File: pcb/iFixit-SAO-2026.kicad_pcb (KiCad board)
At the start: 2 copper layers, 82.6 x 83.8 mm, 11 parts

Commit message: Update from our April 29th meeting.
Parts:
- added R1: 65R, Resistor_SMD:R_1206_3216Metric_Pad1.30x1.75mm_HandSolder, B.Cu at (108.6, 172.3)
- added R2: 65Ω, Resistor_SMD:R_1206_3216Metric_Pad1.30x1.75mm_HandSolder, B.Cu at (108.6, 168.3)
- added TP1: SAO Tether, TestPoint:TestPoint_Keystone_5019_Miniature, B.Cu at (86.7, 158.4)
- added U1: ATtiny1604-SS, Package_SO:SOIC-14_3.9x8.7mm_P1.27mm, B.Cu at (111.4, 147.7)
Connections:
- D1 pad 1: unconnected-(D1-K-Pad1) -> Net-(D1-K)
- D1 pad 2: unconnected-(D1-A-Pad2) -> Net-(D1-A)
- D2 pad 1: unconnected-(D2-K-Pad1) -> Net-(D2-K)
- D2 pad 2: unconnected-(D2-A-Pad2) -> Net-(D2-A)
- LED1 pad 2: unconnected-(LED1-VDD-Pad2) -> Net-(LED1-VDD)
- LED1 pad 4: unconnected-(LED1-GND-Pad4) -> GND
- LED2 pad 2: unconnected-(LED2-VDD-Pad2) -> Net-(LED1-VDD)
- LED2 pad 4: unconnected-(LED2-GND-Pad4) -> GND
- LED3 pad 2: unconnected-(LED3-VDD-Pad2) -> Net-(LED1-VDD)
- LED3 pad 4: unconnected-(LED3-GND-Pad4) -> GND
- LED4 pad 2: unconnected-(LED4-VDD-Pad2) -> Net-(LED1-VDD)
- LED4 pad 4: unconnected-(LED4-GND-Pad4) -> GND
- LED5 pad 2: unconnected-(LED5-VDD-Pad2) -> Net-(LED1-VDD)
- LED5 pad 4: unconnected-(LED5-GND-Pad4) -> GND
- LED6 pad 2: unconnected-(LED6-VDD-Pad2) -> Net-(LED1-VDD)
- LED6 pad 4: unconnected-(LED6-GND-Pad4) -> GND
- LED7 pad 2: unconnected-(LED7-VDD-Pad2) -> Net-(LED1-VDD)
- LED7 pad 4: unconnected-(LED7-GND-Pad4) -> GND
- SAO1 pad 1: unconnected-(SAO1-3.3V-Pad1) -> Net-(LED1-VDD)
- SAO1 pad 2: unconnected-(SAO1-GND-Pad2) -> GND
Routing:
- net Net-(LED1-VDD): track 0.00 -> 69.8 mm, vias 0 -> 3
- net Net-(D2-A): track 0.00 -> 24.4 mm
- net Net-(D1-A): track 0.00 -> 20.3 mm
- net Net-(D2-K): track 0.00 -> 3.95 mm
- net Net-(D1-K): track 0.00 -> 3.59 mm
- added copper zone on B.Cu, net GND
- added copper zone on F.Cu, net GND

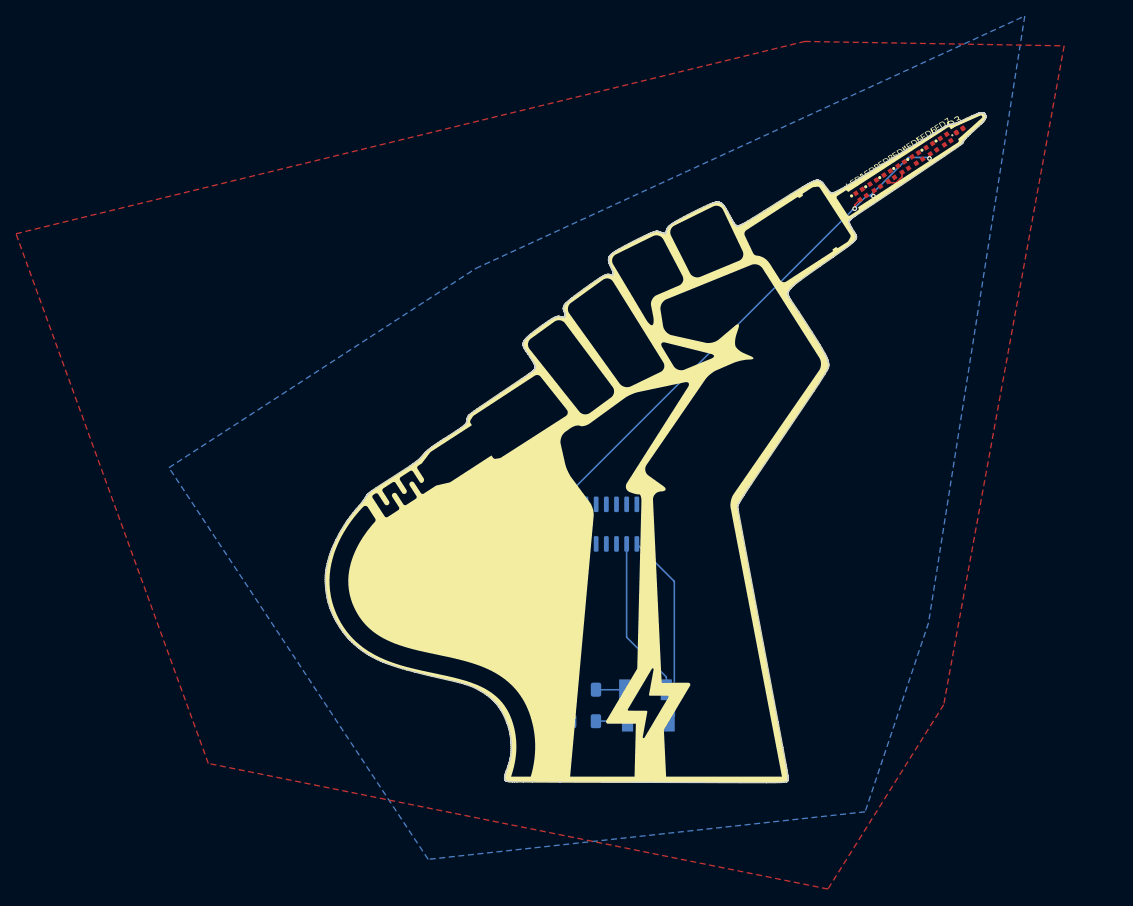
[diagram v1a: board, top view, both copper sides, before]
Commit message: A complete prototype of v0 of the badge, ready for production and assembly. Cleaned up the schematic quite a bit, added teh UDPI programming pads, and updated the SK6508 footprint silkscreen.
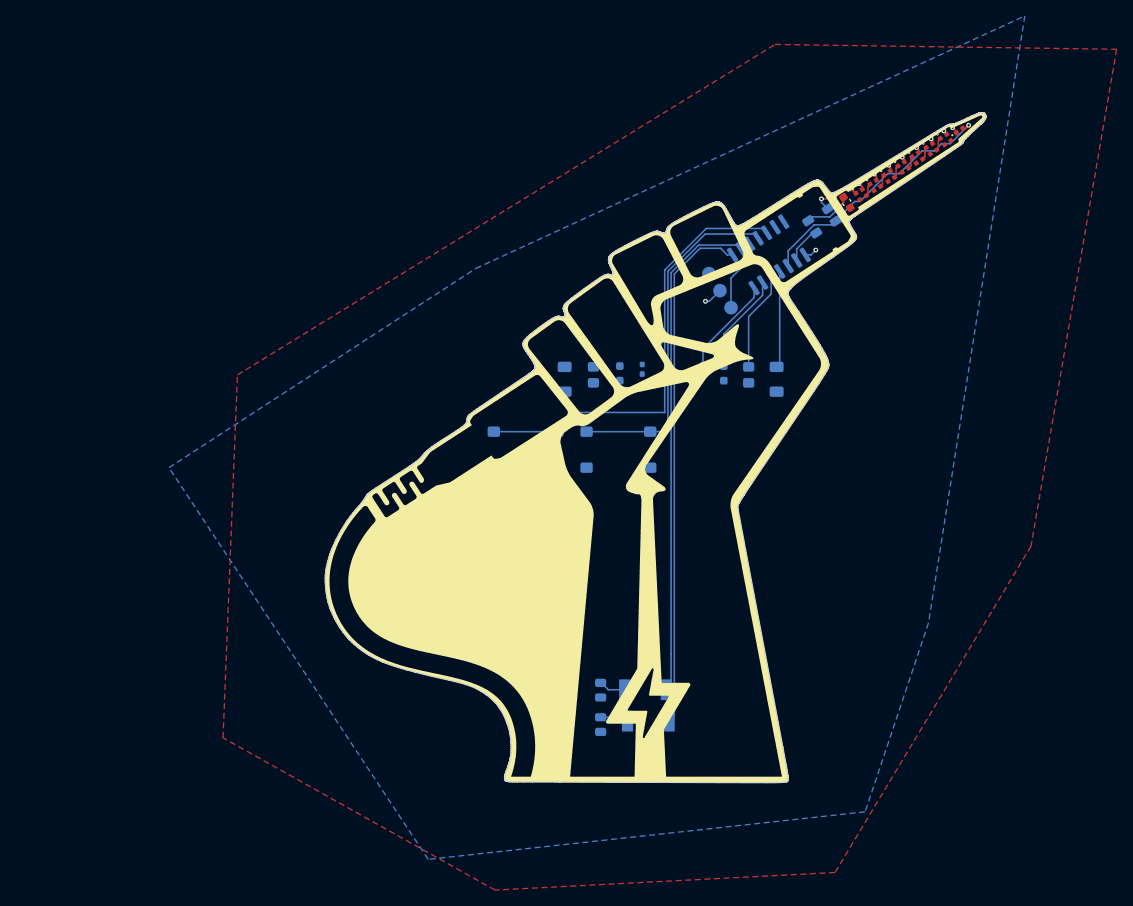
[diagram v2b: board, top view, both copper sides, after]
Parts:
- added C1: 0.1uF, Capacitor_SMD:C_0603_1608Metric, F.Cu at (141.5, 107.5)
- added C2: 0.1uF, Capacitor_SMD:C_0603_1608Metric, B.Cu at (86.7, 158.5)
- added J1: Conn_01x03_Pin, iFixit-SAO-2026:UDPI_1x03_P2.54mm_SMT, B.Cu at (127.0, 120.6)
- added R10: 0R, Resistor_SMD:R_0603_1608Metric_Pad0.98x0.95mm_HandSolder, B.Cu at (113.1, 128.8)
- added R11: R, Resistor_SMD:R_0402_1005Metric_Pad0.72x0.64mm_HandSolder, B.Cu at (123.5, 128.3)
- added R12: 0R, Resistor_SMD:R_0402_1005Metric_Pad0.72x0.64mm_HandSolder, B.Cu at (115.9, 128.3)
- added R3: 500R, Resistor_SMD:R_0805_2012Metric, B.Cu at (139.6, 109.0)
- added R4: 65R, Resistor_SMD:R_0805_2012Metric, B.Cu at (137.1, 110.5)
- added R5: R, Resistor_SMD:R_1206_3216Metric_Pad1.30x1.75mm_HandSolder, B.Cu at (132.7, 129.6)
- added R6: 0R, Resistor_SMD:R_1206_3216Metric_Pad1.30x1.75mm_HandSolder, B.Cu at (106.2, 129.6)
- added R7: R, Resistor_SMD:R_0805_2012Metric_Pad1.20x1.40mm_HandSolder, B.Cu at (129.2, 129.0)
- added R8: 0R, Resistor_SMD:R_0805_2012Metric_Pad1.20x1.40mm_HandSolder, B.Cu at (109.8, 129.0)
- added R9: R, Resistor_SMD:R_0603_1608Metric_Pad0.98x0.95mm_HandSolder, B.Cu at (126.1, 128.8)
- added SW1: SW_Push, Button_Switch_SMD:SW_SPST_PTS645Sx43SMTR92, B.Cu at (112.9, 138.3)
- added SW2: SW_Push, Button_Switch_SMD:SW_SPST_PTS645Sx43SMTR92, B.Cu at (101.3, 138.3)
- R1: renamed from R2; footprint Resistor_SMD:R_1206_3216Metric_Pad1.30x1.75mm_HandSolder -> Resistor_SMD:R_0805_2012Metric
- R2: renamed from R1; footprint Resistor_SMD:R_1206_3216Metric_Pad1.30x1.75mm_HandSolder -> Resistor_SMD:R_0805_2012Metric
- moved U1 39.3 mm to (131.7, 114.0), turned to 123 degrees
- moved TP1 20.1 mm to (106.8, 158.5)
- moved R2 2.18 mm to (110.7, 172.7), turned to -90 degrees
- moved R1 2.13 mm to (110.7, 168.4), turned to -90 degrees
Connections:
- net Net-(LED1-VDD) renamed /3V3
- D3 pad 1: unconnected-(D3-K-Pad1) -> GND
- D3 pad 2: unconnected-(D3-A-Pad2) -> Net-(D3-A)
- LED1 pad 1: unconnected-(LED1-DIN-Pad1) -> /Neopixels
- LED1 pad 3: unconnected-(LED1-DOUT-Pad3) -> Net-(LED1-DOUT)
- LED2 pad 1: unconnected-(LED2-DIN-Pad1) -> Net-(LED1-DOUT)
- LED2 pad 3: unconnected-(LED2-DOUT-Pad3) -> Net-(LED2-DOUT)
- LED3 pad 1: unconnected-(LED3-DIN-Pad1) -> Net-(LED2-DOUT)
- LED3 pad 3: unconnected-(LED3-DOUT-Pad3) -> Net-(LED3-DOUT)
- LED4 pad 1: unconnected-(LED4-DIN-Pad1) -> Net-(LED3-DOUT)
- LED4 pad 3: unconnected-(LED4-DOUT-Pad3) -> Net-(LED4-DOUT)
- LED5 pad 1: unconnected-(LED5-DIN-Pad1) -> Net-(LED4-DOUT)
- LED5 pad 3: unconnected-(LED5-DOUT-Pad3) -> Net-(LED5-DOUT)
- LED6 pad 1: unconnected-(LED6-DIN-Pad1) -> Net-(LED5-DOUT)
- LED6 pad 3: unconnected-(LED6-DOUT-Pad3) -> Net-(LED6-DOUT)
- LED7 pad 1: unconnected-(LED7-DIN-Pad1) -> Net-(LED6-DOUT)
- U1 pad 10: unconnected-(U1-~{RESET}/PA0-Pad10) -> Net-(J1-Pin_1)
- U1 pad 11: unconnected-(U1-PA1-Pad11) -> /BTN1
- U1 pad 12: unconnected-(U1-PA2-Pad12) -> /BTN2
- U1 pad 2: unconnected-(U1-PA4-Pad2) -> Net-(U1-PA4)
- U1 pad 3: unconnected-(U1-PA5-Pad3) -> Net-(U1-PA5)
- U1 pad 4: unconnected-(U1-PA6-Pad4) -> /1206
- U1 pad 5: unconnected-(U1-PA7-Pad5) -> /0805
- U1 pad 6: unconnected-(U1-PB3-Pad6) -> /0603
- U1 pad 7: unconnected-(U1-PB2-Pad7) -> /0402
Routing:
- net /3V3: track 69.8 -> 11.2 mm, vias 3 -> 2
- net /BTN2: track 0.00 -> 55.3 mm
- net /BTN1: track 0.00 -> 43.6 mm
- net Net-(D1-A): track 20.3 -> 63.1 mm
- net Net-(D2-A): track 24.4 -> 65.1 mm
- net Net-(D3-A): track 0.00 -> 25.9 mm, vias 0 -> 1
- net /0603: track 0.00 -> 12.4 mm
- net /0805: track 0.00 -> 12.4 mm
- net /0402: track 0.00 -> 12.2 mm
- net /1206: track 0.00 -> 12.1 mm
- net Net-(U1-PA5): track 0.00 -> 9.39 mm
- net Net-(J1-Pin_1): track 0.00 -> 8.94 mm
- net GND: track 0.00 -> 7.44 mm, vias 0 -> 9
- net /Neopixels: track 0.00 -> 6.46 mm, vias 0 -> 1
- net Net-(U1-PA4): track 0.00 -> 4.70 mm
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- added copper zone on F.Cu, net /3V3
- removed copper zone on F.Cu, net GND
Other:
- board text added: "iFixit SAO 2026 v0"

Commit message: Version v0 sent for PCBA prototype.
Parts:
- R1: value 65Ω -> 65R
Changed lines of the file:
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@@
 			(net "unconnected-(U1-PA3-Pad13)")
 			(pinfunction "PA3_13")
-			(pintype "bidirectional")
+			(pintype "bidirectional+no_connect")
 		)
 		(pad "14" smd roundrect
@@
 			)
 		)
-		(property "Value" "65Ω"
+		(property "Value" "65R"
 			(at 0 -1.65 90)
 			(layer "B.Fab")

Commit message: Version 0.1 (fixed split ground planes, removed button, added new graphics); initial commit of firmware; adding individual pcb layer svgs
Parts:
- removed SW2: SW_Push, Button_Switch_SMD:SW_SPST_PTS645Sx43SMTR92
- moved SW1 11.6 mm to (101.3, 138.3)
- renumbered J1 to UPDI
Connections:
- U1 pad 12: /BTN2 -> unconnected-(U1-PA2-Pad12)
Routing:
- net /BTN2: track 55.3 -> 0.00 mm
- net /BTN1: track 43.6 -> 55.5 mm
- net /0402: track 12.2 -> 17.4 mm
- net /0603: track 12.4 -> 15.3 mm
- net /0805: track 12.4 -> 12.9 mm
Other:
- board text added: "Move these..."
- board text added: "Powering Your Right To Repair"
- board text added: "for a treat."
- board text added: "github.com/NerdFlare/iFixit-SAO-2026"
- board text added: "ifixit.com/FixHub"
- board text added: "mode"
- board text added: "over here..."
- board text removed: "iFixit SAO 2026 v0"
